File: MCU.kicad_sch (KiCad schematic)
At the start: 28 parts, among them Q1 L8050QLT1G, Q2 L8050QLT1G, SW1 SW_Push, SW2 SW_Push, U4 CP2102N-Axx-xQFN28, U5 ESP32-S3-WROOM-1-N16

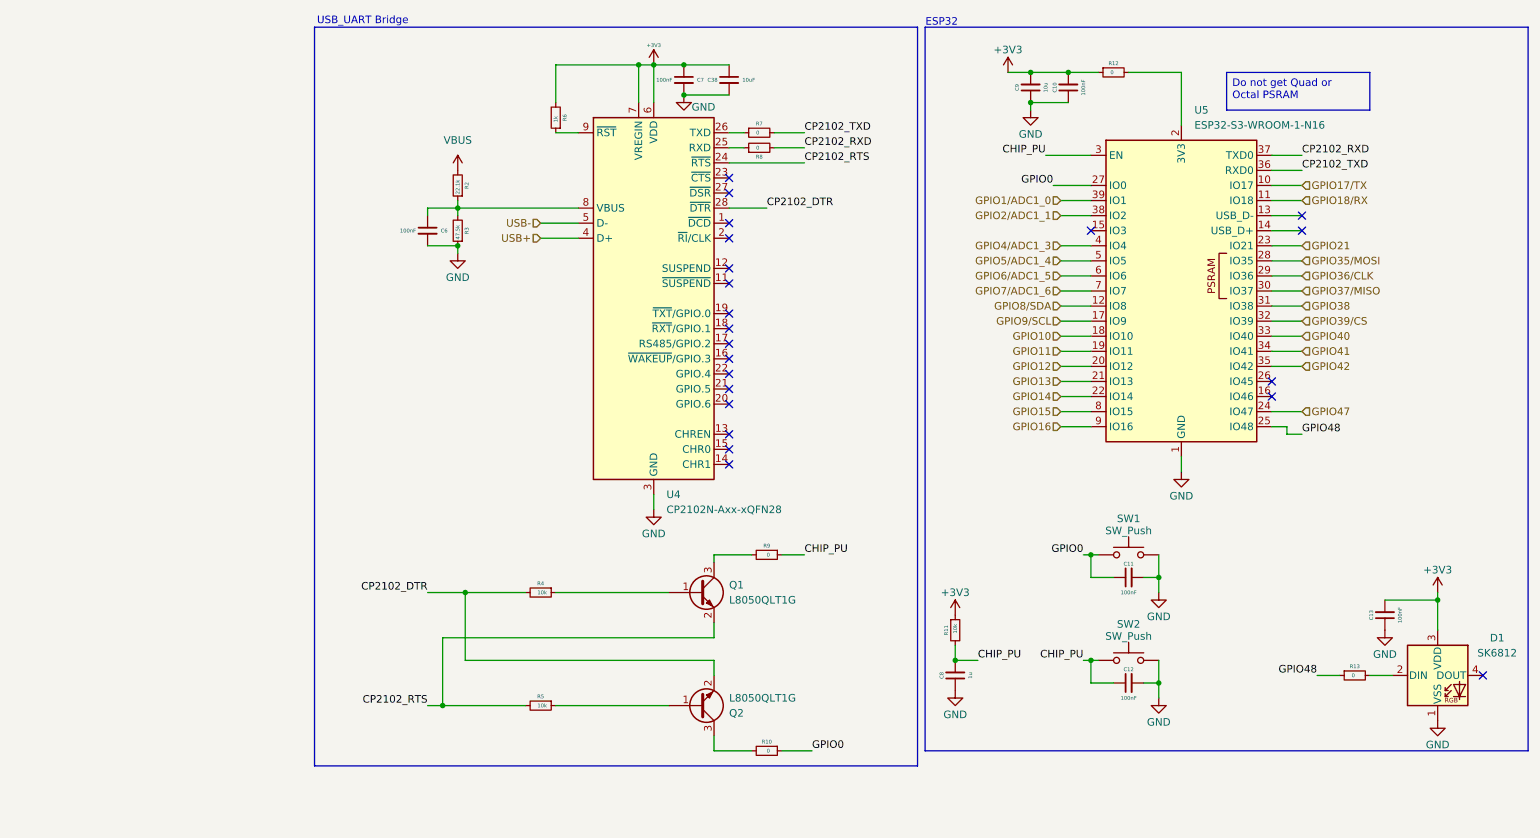
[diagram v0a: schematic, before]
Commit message: Schematic updated for V2.0, updating PCB now
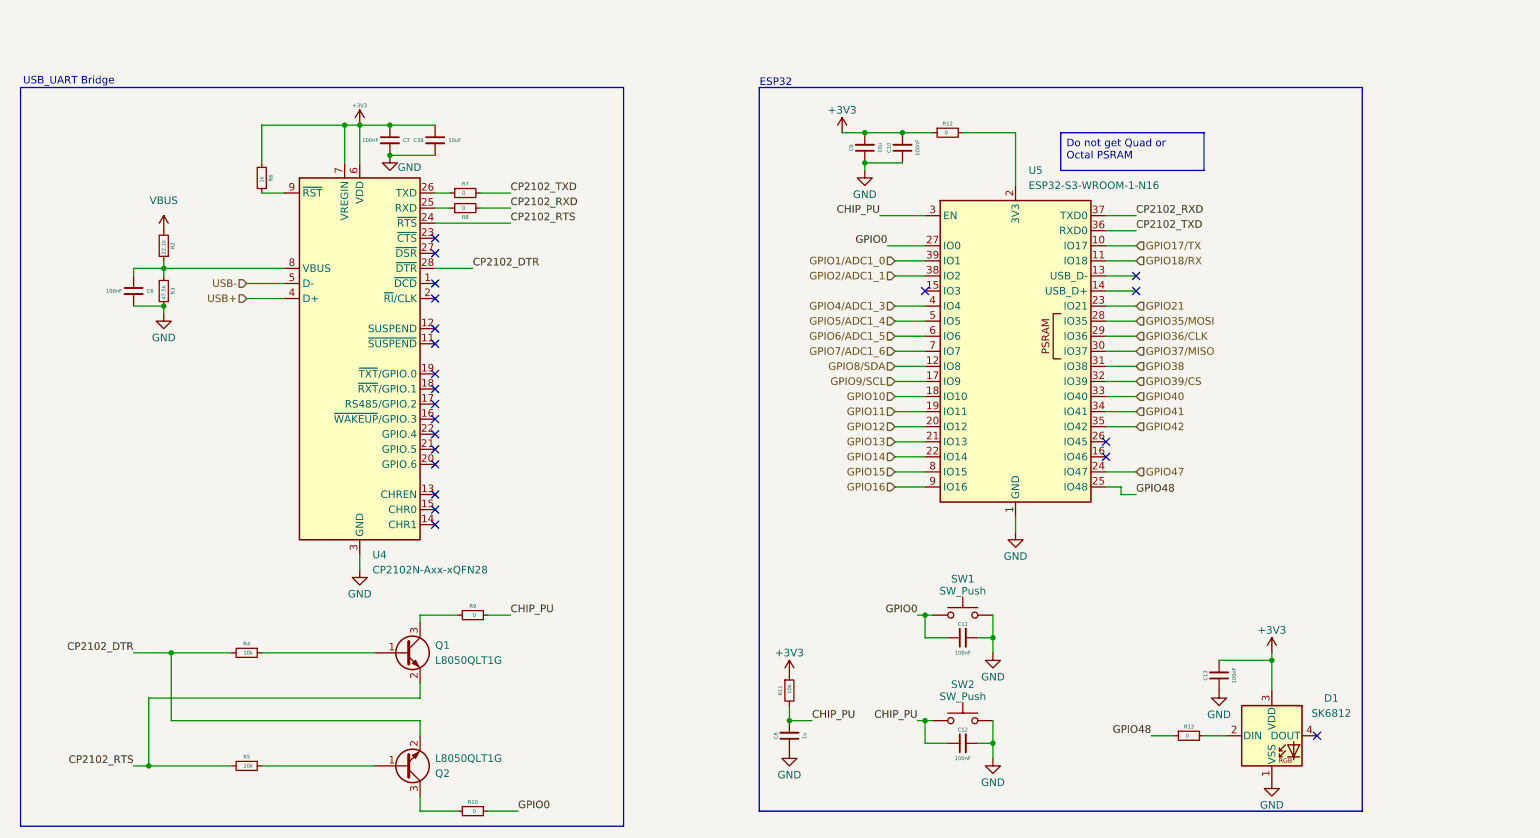
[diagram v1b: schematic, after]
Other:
- moved on the sheet: C10, C11, C12, C13, C38, C6, C7, C8, C9, D1, Q1, Q2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

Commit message: Version 2 sent to JLC
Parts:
- removed C13: 100nF, Capacitor_SMD:C_0402_1005Metric, symbol Device:C_Small
- removed D1: SK6812, LED_SMD:LED_SK6812_PLCC4_5.0x5.0mm_P3.2mm, symbol LED:SK6812
- added D1: LED, LED_SMD:LED_0603_1608Metric, symbol Device:LED
- R13: value 0 -> 280
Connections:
- net GND: now also D1.1 (K)
- net at R13.2: now also D1.2 (A)
- net GPIO48: no longer names the net of R13.1, U5.25 (IO48)
- no-connect marks 22 -> 21
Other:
- moved on the sheet: R13
